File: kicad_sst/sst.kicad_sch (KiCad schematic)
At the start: 0 parts

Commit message: Almsost done with the sceme: part that connected to MCU is connected
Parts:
- added C? (x5): C, symbol sst:C
- added DA?: LM7805_TO220, Package_TO_SOT_THT:TO-220-3_Vertical, symbol sst:LM7805_TO220
- added DD?: ATmega328-P, Package_DIP:DIP-28_W7.62mm, symbol sst:ATmega328-P
- added HA?: Buzzer, symbol sst:Buzzer
- added HL?: HL_LED, symbol sst:HL_LED
- added R? (x7): R, symbol sst:R
- added R? (x3): R_POT, symbol sst:R_POT
- added R?: R_POT, Potentiometer_SMD:Potentiometer_ACP_CA6-VSMD_Vertical, symbol sst:R_POT
- added SA?: ~, symbol sst:4П2Н
- added SA?: SA_SPDT, symbol sst:SA_SPDT
- added VD?: VD_Schottky, symbol sst:VD_Schottky
- added VT?: 2П7240, Package_SO:SOIC-8_3.9x4.9mm_P1.27mm, symbol sst:2П7240
- added X?: CONN_8, symbol Connector_Generic_GOST:CONN_8
- added X?: CONN_2, symbol Connector_Generic_GOST:CONN_2
- added XS? (x2): CONN_12, symbol Connector_Generic_GOST:CONN_12
- added XS?: CONN_6, symbol Connector_Generic_GOST:CONN_6
- added ZQ?: ZQ_CRYSTAL, symbol sst:ZQ_CRYSTAL
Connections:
- new net: C?.1, DA?.1 (IN), VD?.1 (K)
- new net: VD?.2 (A), X?.1
- new net: DD?.27 (PC4), R?.1, R?.1
- new net: C?.1, C?.1, DA?.3 (OUT), SA?.
- new net: C?.2, DD?.17 (PB3), DD?.9 (XTAL1/PB6), XS?.4, XS?.7, ZQ?.1
- new net: C?.2, DD?.10 (XTAL2/PB7), ZQ?.2
- new net: R?.1, R?.2
- new net: C?.1, DD?.8 (GND)
- new net: DD?.4 (PD2), R?.1, VT?.2 (G1)
- new net: DD?.12 (PD6), XS?.1
- new net: DD?.18 (PB4), XS?.1, XS?.2
- new net: DD?.11 (PD5), XS?.7
- new net: DD?.13 (PD7), XS?.8
- new net: DD?.26 (PC3), R?.2
- new net: DD?.16 (PB2), XS?.1
- new net: DD?.14 (PB0), XS?.2
- new net: DD?.15 (PB1), XS?.8
- new net: HA?.2 (-), HL?.1 (K), VT?.5 (D1), VT?.6 (D1)
- new net: HL?.2 (A), R?.1
- new net: DD?.6 (PD4), SA?.
- new net: DD?.19 (EPB5), XS?.3
- new net: DD?.1 (~{RESET}/PC6), XS?.5
- new net: DD?.23 (PC0), R?.2
- new net: DD?.2 (PD0), R?.1, X?.1, X?.5
- new net: DD?.3 (PD1), R?.1, X?.2, X?.6
- new net: HA?.1 (+), SA?.1
- new net +2V5: DD?.21 (AREF), R?.1, R?.1, R?.1, R?.1
- new net +5V: DD?.20 (AVCC), DD?.7 (VCC), R?.2, R?.2, R?.2, SA?.2, X?.4, X?.7, XS?.2
- new net +BATT: R?.2, SA?., XS?.10, XS?.10, XS?.3, XS?.3, XS?.4, XS?.4, XS?.9, XS?.9
- new net GND: C?.2, C?.2, C?.2, DA?.2 (GND), DD?.24 (PC1), DD?.25 (PC2), R?.2, R?.2, R?.2, R?.2, R?.3, R?.3, R?.3, R?.3, SA?., VT?.1 (S1), X?.2, X?.3, X?.8, XS?.11, XS?.11, XS?.12, XS?.12, XS?.5, XS?.5, XS?.6, XS?.6, XS?.6

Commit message: Done with schematic
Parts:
- added C?: C, symbol sst:C
- added R? (x2): R, symbol sst:R
- added VD? (x2): VD, symbol sst:VD
- gave numbers to parts that had none: 1
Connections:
- net +2V5: now also C?.1, R?.2, VD?.1 (K)
- net +5V: now also R?.1, R?.2, VD?.1 (K)
- net +BATT: now also R?.1
- net GND: now also C?.2, VD?.2 (A), VD?.2 (A)

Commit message: Fixes to the schematics
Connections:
- net GND: now also DD?.22 (GND)
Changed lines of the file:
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@@
 	(wire
 		(pts
-			(xy 38.1 38.1) (xy 38.1 190.5)
+			(xy 38.1 36.83) (xy 38.1 190.5)
 		)
 		(stroke
@@
 	(wire
 		(pts
-			(xy 101.6 16.51) (xy 101.6 38.1)
-		)
-		(stroke
-			(width 0)
-			(type default)
-		)
-	)
-	(wire
-		(pts
 			(xy 208.28 109.22) (xy 208.28 149.86)
 		)
@@
 	(wire
 		(pts
-			(xy 101.6 38.1) (xy 38.1 38.1)
+			(xy 101.6 36.83) (xy 38.1 36.83)
 		)
 		(stroke
@@
 		)
 		(stroke
+			(width 0)
+			(type default)
+		)
+	)
+	(wire
+		(pts
+			(xy 101.6 16.322) (xy 101.6 36.83)
+		)
+		(stroke

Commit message: Сделлал аннотацию схемы
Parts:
- XS3: renamed from X?; PIN2 2 -> 2a; PIN3 3 -> 3a; PIN4 4 -> 4a; PIN5 5 -> 1b; PIN6 6 -> 2b; PIN7 7 -> 3b; PIN8 8 -> 4b
- gave numbers to parts that had none: 34
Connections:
- net GND: now also C5.1, C6.1, DD1.8 (GND)
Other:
- moved on the sheet: XS5

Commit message: Linked footprints to schematics
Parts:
- C1, C4: footprint (none) -> Capacitor_THT:CP_Radial_D8.0mm_P2.50mm
- C2: footprint (none) -> Capacitor_THT:CP_Radial_D8.0mm_P3.50mm
- C3: footprint (none) -> Capacitor_THT:CP_Radial_D5.0mm_P2.00mm
- C5, C6: footprint (none) -> Capacitor_THT:CP_Radial_D5.0mm_P2.50mm
- HA1: footprint (none) -> Buzzer_Beeper:Buzzer_TDK_PS1240P02BT_D12.2mm_H6.5mm
- HL1: footprint (none) -> LED_THT:LED_D3.0mm
- R1, R10, R11, R12, R13, R2, R3, R4, R9: footprint (none) -> Resistor_THT:R_Axial_DIN0207_L6.3mm_D2.5mm_P7.62mm_Horizontal
- R5: footprint Potentiometer_SMD:Potentiometer_ACP_CA6-VSMD_Vertical -> Potentiometer_THT:Potentiometer_TT_P0915N
- R6, R7, R8: footprint (none) -> Potentiometer_THT:Potentiometer_TT_P0915N
- SA1: footprint (none) -> Button_Switch_THT:SW_CK_JS202011CQN_DPDT_Straight
- SA2: footprint (none) -> Button_Switch_THT:SW_Slide_SPDT_Angled_CK_OS102011MA1Q
- VD1, VD2, VD3: footprint (none) -> Diode_THT:D_5KPW_P12.70mm_Horizontal
- VT1: footprint Package_SO:SOIC-8_3.9x4.9mm_P1.27mm -> Package_TO_SOT_THT:TO-92
- XS1: footprint (none) -> Connector_BarrelJack:BarrelJack_Horizontal
- XS2, XS5: footprint (none) -> Connector_PinHeader_2.54mm:PinHeader_2x06_P2.54mm_Vertical
- XS3: footprint (none) -> Connector_PinSocket_2.54mm:PinSocket_2x04_P2.54mm_Vertical; PIN2 2a -> 2; PIN3 3a -> 3; PIN4 4a -> 4; PIN5 1b -> 5; PIN6 2b -> 6; PIN7 3b -> 7; PIN8 4b -> 8
- XS4: footprint (none) -> Connector_PinHeader_2.54mm:PinHeader_2x05_P2.54mm_Vertical; PIN2 VCC -> 2; PIN3 SCK -> 3; PIN4 MOSI -> 4; PIN5 RST -> 5; PIN6 GND -> 6
- ZQ1: footprint (none) -> Crystal:Crystal_HC49-U_Vertical
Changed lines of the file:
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@@
 			)
 		)
-		(property "Footprint" ""
+		(property "Footprint" "Capacitor_THT:CP_Radial_D8.0mm_P2.50mm"
 			(at 71.76 254.762 0)
 			(effects
@@
 			)
 		)
-		(property "Footprint" ""
+		(property "Footprint" "Diode_THT:D_5KPW_P12.70mm_Horizontal"
 			(at 78.74 261.62 0)
 			(effects
@@
 			)
 		)
-		(property "Footprint" ""
+		(property "Footprint" "Resistor_THT:R_Axial_DIN0207_L6.3mm_D2.5mm_P7.62mm_Horizontal"
 			(at 349.758 164.846 0)
 			(effects
@@
 			)
 		)
-		(property "Footprint" ""
+		(property "Footprint" "Capacitor_THT:CP_Radial_D8.0mm_P3.50mm"
 			(at 85.598 269.88 0)
 			(effects
@@
 			)
 		)
-		(property "Footprint" ""
+		(property "Footprint" "Capacitor_THT:CP_Radial_D8.0mm_P2.50mm"
 			(at 149.098 276.23 0)
 			(effects
@@
 			)
 		)
-		(property "Footprint" ""
+		(property "Footprint" "Crystal:Crystal_HC49-U_Vertical"
 			(at 178.308 42.992 0)
 			(effects
@@
 			)
 		)
-		(property "Footprint" ""
+		(property "Footprint" "Resistor_THT:R_Axial_DIN0207_L6.3mm_D2.5mm_P7.62mm_Horizontal"
 			(at 348.742 124.714 0)
 			(effects
@@
 			)
 		)
-		(property "Footprint" ""
+		(property "Footprint" "Capacitor_THT:CP_Radial_D5.0mm_P2.50mm"
 			(at 159.258 33.688 0)
 			(effects
@@
 			)
 		)
-		(property "Footprint" ""
+		(property "Footprint" "Capacitor_THT:CP_Radial_D5.0mm_P2.50mm"
 			(at 197.358 33.688 0)
 			(effects
@@
 			)
 		)
-		(property "Footprint" ""
+		(property "Footprint" "Potentiometer_THT:Potentiometer_TT_P0915N"
 			(at 272.542 143.764 0)
 			(effects
@@
 			)
 		)
-		(property "Footprint" ""
+		(property "Footprint" "Resistor_THT:R_Axial_DIN0207_L6.3mm_D2.5mm_P7.62mm_Horizontal"
 			(at 384.048 220.726 0)
 			(effects
@@
 			)
 		)
-		(property "Footprint" ""
+		(property "Footprint" "Connector_PinHeader_2.54mm:PinHeader_2x06_P2.54mm_Vertical"
 			(at 160.02 186.69 0)
 			(effects
@@
 			)
 		)
-		(property "Footprint" ""
+		(property "Footprint" "Resistor_THT:R_Axial_DIN0207_L6.3mm_D2.5mm_P7.62mm_Horizontal"
 			(at 348.742 146.304 0)
 			(effects
@@
 			)
 		)
-		(property "Footprint" ""
+		(property "Footprint" "Diode_THT:D_5KPW_P12.70mm_Horizontal"
 			(at 67.31 236.22 0)
 			(effects
@@
 			)
 		)
-		(property "Footprint" "Potentiometer_SMD:Potentiometer_ACP_CA6-VSMD_Vertical"
+		(property "Footprint" "Potentiometer_THT:Potentiometer_TT_P0915N"
 			(at 233.172 143.764 0)
 			(effects
@@
 			)
 		)
-		(property "Footprint" ""
+		(property "Footprint" "Connector_PinHeader_2.54mm:PinHeader_2x06_P2.54mm_Vertical"
 			(at 342.9 11.43 0)
 			(effects
@@
 			)
 		)
-		(property "Footprint" ""
+		(property "Footprint" "LED_THT:LED_D3.0mm"
 			(at 370.84 194.3024 0)
 			(effects
@@
 			)
 		)
-		(property "Footprint" ""
+		(property "Footprint" "Potentiometer_THT:Potentiometer_TT_P0915N"
 			(at 253.492 143.764 0)
 			(effects
@@
 			)
 		)
-		(property "Footprint" ""
+		(property "Footprint" "Button_Switch_THT:SW_CK_JS202011CQN_DPDT_Straight"
 			(at 181.356 270.002 0)
 			(effects
@@
 			)
 		)
-		(property "Footprint" ""
+		(property "Footprint" "Resistor_THT:R_Axial_DIN0207_L6.3mm_D2.5mm_P7.62mm_Horizontal"
 			(at 376.682 174.244 0)
 			(effects
@@
 			)
 		)
-		(property "Footprint" ""
+		(property "Footprint" "Connector_PinHeader_2.54mm:PinHeader_2x05_P2.54mm_Vertical"
 			(at 303.53 78.74 0)
 			(effects
@@
 			)
 		)
-		(property "Description" "MISO"
+		(property "Description" "1"
 			(at 318.77 88.9 0)
 			(effects
@@
 			)
 		)
-		(property "PIN2" "VCC"
+		(property "PIN2" "2"
 			(at 319.532 93.98 0)
 			(effects
@@
 			)
 		)
-		(property "PIN3" "SCK"
+		(property "PIN3" "3"
 			(at 319.786 98.806 0)
 			(effects
@@
 			)
 		)
-		(property "PIN4" "MOSI"
+		(property "PIN4" "4"
 			(at 319.278 104.394 0)
 			(effects
@@
 			)
 		)
-		(property "PIN5" "RST"
+		(property "PIN5" "5"
 			(at 320.04 109.22 0)
 			(effects
@@
 			)
 		)
-		(property "PIN6" "GND"
+		(property "PIN6" "6"
 			(at 319.532 114.3 0)
 			(effects
@@
 			)
 		)
-		(property "Footprint" ""
+		(property "Footprint" "Potentiometer_THT:Potentiometer_TT_P0915N"
 			(at 291.592 143.764 0)
 			(effects
@@
 			)
 		)
-		(property "Footprint" ""
+		(property "Footprint" "Resistor_THT:R_Axial_DIN0207_L6.3mm_D2.5mm_P7.62mm_Horizontal"
 			(at 202.692 235.204 0)
 			(effects
@@
 			)
 		)
-		(property "Footprint" ""
+		(property "Footprint" "Connector_PinSocket_2.54mm:PinSocket_2x04_P2.54mm_Vertical"
 			(at 250.19 180.34 0)
 			(effects
@@
 			)
 		)
-		(property "Description" "1a"
+		(property "Description" "1"
 			(at 265.938 191.008 0)
 			(effects
@@
 			)
 		)
-		(property "PIN2" "2a"
+		(property "PIN2" "2"
 			(at 266.192 195.58 0)
 			(effects
@@
 			)
 		)
-		(property "PIN3" "3a"
+		(property "PIN3" "3"
 			(at 265.938 200.66 0)
 			(effects
@@
 			)
 		)
-		(property "PIN4" "4a"
+		(property "PIN4" "4"
 			(at 266.192 205.74 0)
 			(effects
@@
 			)
 		)
-		(property "PIN5" "1b"
+		(property "PIN5" "5"
 			(at 265.938 211.582 0)
 			(effects
@@
 			)
 		)
-		(property "PIN6" "2b"
+		(property "PIN6" "6"
 			(at 266.192 216.154 0)
 			(effects
@@
 			)
 		)
-		(property "PIN7" "3b"
+		(property "PIN7" "7"
 			(at 266.192 220.98 0)
 			(effects
@@
 			)
 		)
-		(property "PIN8" "4b"
+		(property "PIN8" "8"
 			(at 265.938 226.568 0)
 			(effects
@@
 			)
 		)
-		(property "Footprint" ""
+		(property "Footprint" "Resistor_THT:R_Axial_DIN0207_L6.3mm_D2.5mm_P7.62mm_Horizontal"
 			(at 48.006 235.712 0)
 			(effects
@@
 			)
 		)
-		(property "Footprint" "Package_SO:SOIC-8_3.9x4.9mm_P1.27mm"
+		(property "Footprint" "Package_TO_SOT_THT:TO-92"
 			(at 392.43 224.79 0)
 			(effects
@@
 			)
 		)
-		(property "Footprint" ""
+		(property "Footprint" "Diode_THT:D_5KPW_P12.70mm_Horizontal"
 			(at 68.58 215.9 0)
 			(effects
@@
 			)
 		)
-		(property "Footprint" ""
+		(property "Footprint" "Capacitor_THT:CP_Radial_D5.0mm_P2.00mm"
 			(at 132.588 276.23 0)
 			(effects
@@
 			)
 		)
-		(property "Footprint" ""
+		(property "Footprint" "Button_Switch_THT:SW_Slide_SPDT_Angled_CK_OS102011MA1Q"
 			(at 393.7 183.896 0)
 			(effects
@@
 			)
 		)
-		(property "Footprint" ""
+		(property "Footprint" "Resistor_THT:R_Axial_DIN0207_L6.3mm_D2.5mm_P7.62mm_Horizontal"
 			(at 45.466 215.392 0)
 			(effects
@@
 			)
 		)
-		(property "Footprint" ""
+		(property "Footprint" "Resistor_THT:R_Axial_DIN0207_L6.3mm_D2.5mm_P7.62mm_Horizontal"
 			(at 215.392 235.204 0)
 			(effects
@@
 			)
 		)
-		(property "Footprint" ""
+		(property "Footprint" "Buzzer_Beeper:Buzzer_TDK_PS1240P02BT_D12.2mm_H6.5mm"
 			(at 400.605 189.23 0)
 			(effects
@@
 			)
 		)
-		(property "Footprint" ""
+		(property "Footprint" "Connector_BarrelJack:BarrelJack_Horizontal"
 			(at 55.88 251.46 0)
 			(effects

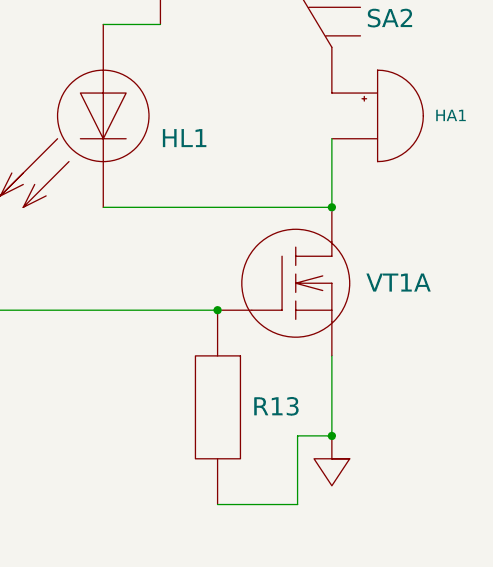
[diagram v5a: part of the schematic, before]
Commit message: Fixes transistor
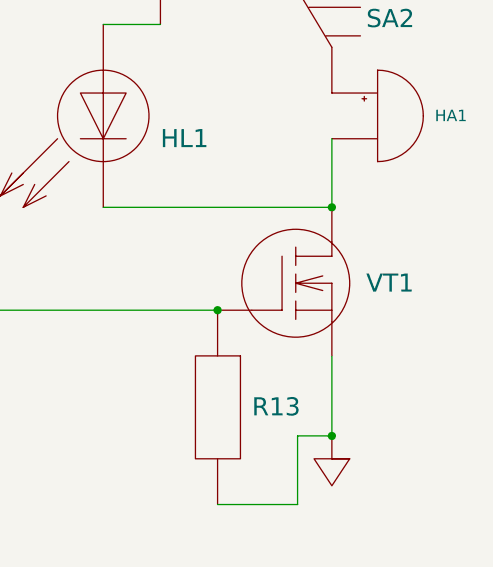
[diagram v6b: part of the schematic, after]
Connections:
- net +BATT: now also SA1.4; no longer SA1.
- net GND: now also SA1.2; no longer SA1.
- net at C3.1, C4.1, DA1.3 (OUT): now also SA1.1; no longer SA1.
- net at HA1.2 (-), HL1.1 (K): now also VT1.3 (D1); no longer VT1.5 (D1), VT1.6 (D1)
- net at DD1.6 (PD4): now also SA1.5; no longer SA1.
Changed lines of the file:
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@@
 			)
 		)
-		(pin ""
-		)
-		(pin ""
-		)
-		(pin ""
-		)
-		(pin ""
-		)
-		(pin ""
-		)
-		(pin ""
+		(pin "3"
+		)
+		(pin "4"
+		)
+		(pin "6"
+		)
+		(pin "1"
+		)
+		(pin "2"
+		)
+		(pin "5"
 		)
 		(instances
@@
 		(pin "3"
 		)
-		(pin "6"
-		)
-		(pin "8"
-		)
 		(pin "2"
 		)
 		(pin "1"
 		)
-		(pin "4"
-		)
-		(pin "5"
-		)
-		(pin "7"
-		)
-		(instances
+		(instances

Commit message: Changed couple of footprints for XS
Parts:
- XS1: footprint Connector_BarrelJack:BarrelJack_Horizontal -> Connector_BarrelJack:BarrelJack_SwitchcraftConxall_RAPC10U_Horizontal
- XS4: footprint Connector_PinHeader_2.54mm:PinHeader_2x05_P2.54mm_Vertical -> Connector_PinHeader_1.00mm:PinHeader_2x03_P1.00mm_Vertical
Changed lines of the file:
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@@
 			)
 		)
-		(property "Footprint" "Connector_PinHeader_2.54mm:PinHeader_2x05_P2.54mm_Vertical"
+		(property "Footprint" "Connector_PinHeader_1.00mm:PinHeader_2x03_P1.00mm_Vertical"
 			(at 303.53 78.74 0)
 			(effects
@@
 			)
 		)
-		(property "Footprint" "Connector_BarrelJack:BarrelJack_Horizontal"
+		(property "Footprint" "Connector_BarrelJack:BarrelJack_SwitchcraftConxall_RAPC10U_Horizontal"
 			(at 55.88 251.46 0)
 			(effects

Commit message: Changed footprint for XS4
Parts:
- XS4: footprint Connector_PinHeader_1.00mm:PinHeader_2x03_P1.00mm_Vertical -> Connector_PinHeader_2.54mm:PinHeader_2x03_P2.54mm_Vertical
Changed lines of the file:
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@@
 			)
 		)
-		(property "Footprint" "Connector_PinHeader_1.00mm:PinHeader_2x03_P1.00mm_Vertical"
+		(property "Footprint" "Connector_PinHeader_2.54mm:PinHeader_2x03_P2.54mm_Vertical"
 			(at 303.53 78.74 0)
 			(effects
